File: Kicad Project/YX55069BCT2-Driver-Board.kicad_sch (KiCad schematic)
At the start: 151 parts, among them J1 10029449-001RLF, Q1 BSS138_C112239, Q2 BSS138_C112239, Q4 BSS138_C112239, SW3 BOOT, SW4 RESET, U1 TC358870XBG(NOK), U10 ESP32-S3R8, U11 GD25Q128EWIGR, U12 USBLC6-2SC6, U13 SN74AXC1T45DCKR, U14 TXS0101DBVR, U15 TPS61165DBVR, U16 TVS0500DRVR, U2 TLV76701DRVR, U3 CH224K, U4 TLV76718DRVR, U5 TLV76728DRVR, U6 TLV76733DRVR, U62 PCA9306DCUR, U63 AP2120N-2.8TRG1, U64 PCA9306DCUR, U7 TLV76701DRVR, U8 ESD7104MUTAG_C2987068, U9 TPS259474LRPWR, X1 ABM8-40.000MHZ-10-D1G-T

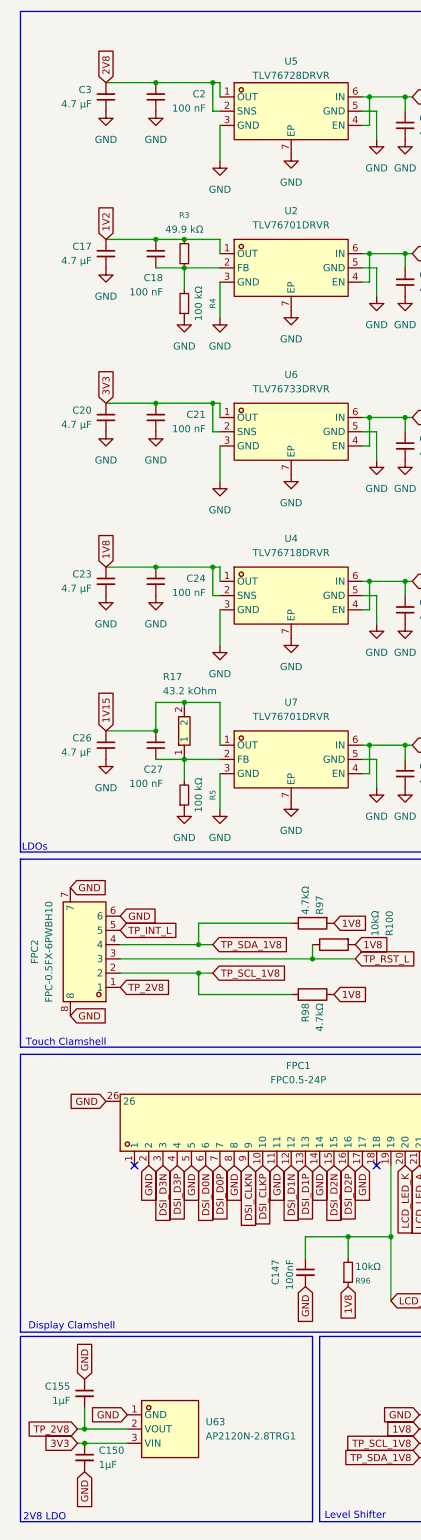
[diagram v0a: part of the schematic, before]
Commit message: wired rest of components, and majority of remaining caps and resistors
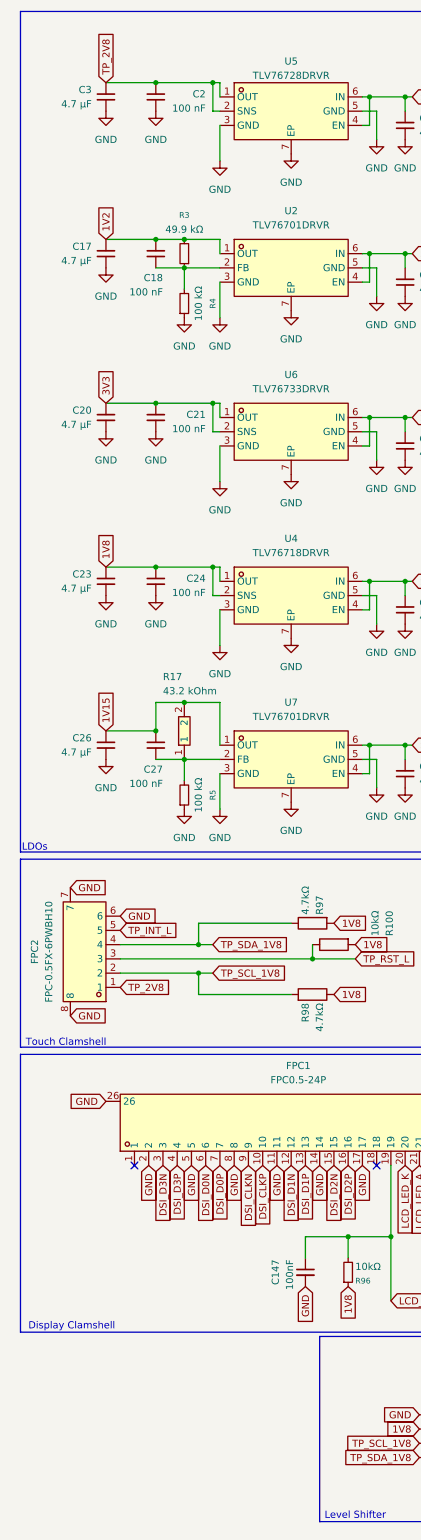
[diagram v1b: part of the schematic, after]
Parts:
- removed C150, C155: 1µF, Capacitor_SMD:C_0603_1608Metric, symbol Device:C_Small
- removed U63: AP2120N-2.8TRG1, slate113:SOT-23-3_L2.9-W1.3-P1.90-LS2.4-BR, symbol slate113:AP2120N-2.8TRG1
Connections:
- net 2V8 is gone; now on net TP_2V8: C2.2, C3.2, U5.1 (OUT), U5.2 (SNS)
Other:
- note removed: "2V8 LDO"

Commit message: fixed most of DRC errors
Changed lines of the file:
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@@
 	(wire
 		(pts
-			(xy 485.14 116.84) (xy 485.14 123.19)
-		)
-		(stroke
-			(width 0)
-			(type default)
-		)
-	)
-	(wire
-		(pts
 			(xy 49.53 127) (xy 49.53 120.65)
 		)
@@
 	(symbol
 		(lib_id "power:GND")
-		(at 485.14 123.19 0)
+		(at 485.14 116.84 0)
 		(unit 1)
 		(body_style 1)
@@
 		(fields_autoplaced yes)
 		(property "Reference" "#PWR037"
-			(at 485.14 129.54 0)
+			(at 485.14 123.19 0)
 			(hide yes)
 			(show_name no)
@@
 		)
 		(property "Value" "GND"
-			(at 485.14 128.27 0)
+			(at 485.14 121.92 0)
 			(show_name no)
 			(do_not_autoplace no)
@@
 		)
 		(property "Footprint" ""
-			(at 485.14 123.19 0)
+			(at 485.14 116.84 0)
 			(hide yes)
 			(show_name no)
@@
 		)
 		(property "Datasheet" ""
-			(at 485.14 123.19 0)
+			(at 485.14 116.84 0)
 			(hide yes)
 			(show_name no)
@@
 		)
 		(property "Description" "Power symbol creates a global label with name \"GND\" , ground"
-			(at 485.14 123.19 0)
+			(at 485.14 116.84 0)
 			(hide yes)
 			(show_name no)

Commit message: add README + production files
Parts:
- C1, C19, C22, C25, C28: LCSC C277499 -> C69335; LCSC Part (none) -> C69335
- C14, C15, C16, C29, C30, C36, C39, C4, C40, C41, C42, C43, C44, C45, C46, C47, C5, C59, C6, C62, C63, C64, C7, C8, C9: LCSC C77044 -> C1591; LCSC Part (none) -> C1591
- C17, C20, C23, C26, C3: LCSC C2857993 -> C69335; LCSC Part (none) -> C69335
- C18, C2, C21, C24, C27, C65: LCSC C2169363 -> C1591; LCSC Part (none) -> C1591
- C31, C33, C34, C35, C48, C58, C69: LCSC Part (none) -> C77044
- C32, C68: LCSC Part (none) -> C52923
- C37, C38: LCSC Part (none) -> C86285
- C49, C50, C51, C52, C61: LCSC Part (none) -> C29936
- C53, C54, C55, C56, C57, C60: LCSC Part (none) -> C23630
- FB1, FB2: LCSC (none) -> C14709; LCSC Part (none) -> C14709
- J1: value 10029449-001RLF -> 10029449-111RLF; LCSC C428493 -> C427307; LCSC Part (none) -> C427307
- U12: LCSC (none) -> C7519; LCSC Part (none) -> C7519
